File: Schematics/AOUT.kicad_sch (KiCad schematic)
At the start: 25 parts, among them J10 Line Out, J5 Inst Out, Q1 Q_NPN_BEC, Q2 Q_NPN_BEC, U4 Opamp_Dual

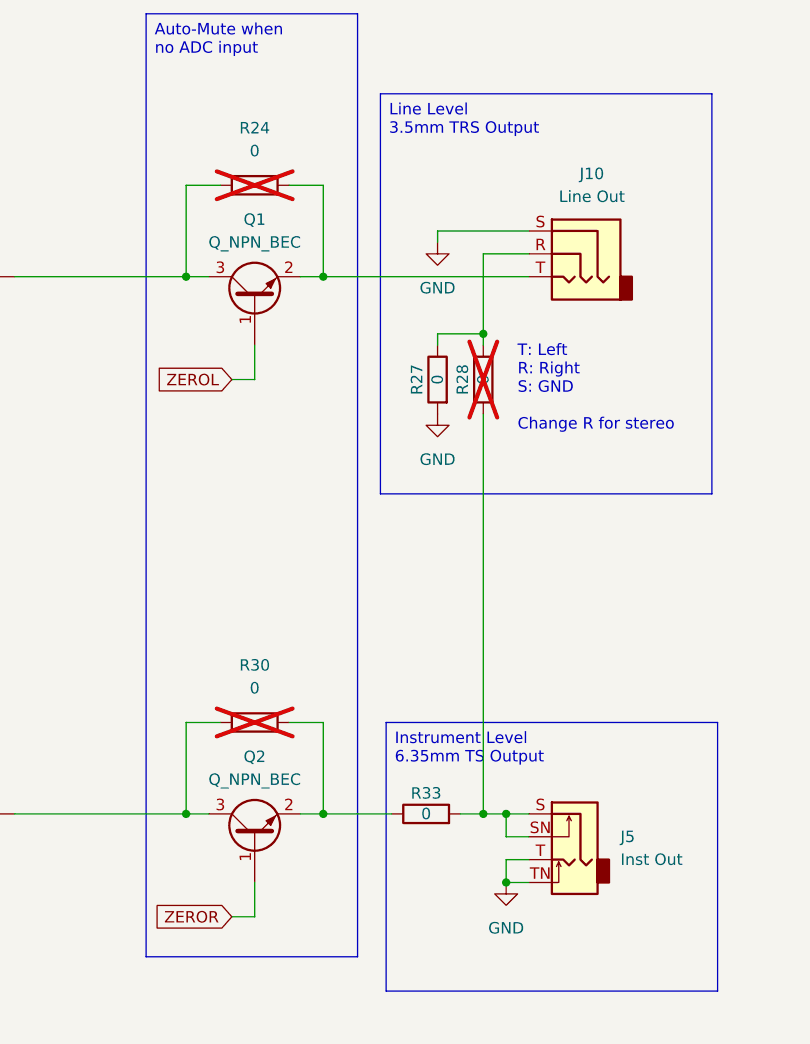
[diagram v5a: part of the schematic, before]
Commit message: Added all footprints, updated PCB
Added footprints using uni available components where possible. Might be necessary to change op-amps as they are large and not made for audio. PCB has a mockup of component placements but probably needs expanded.
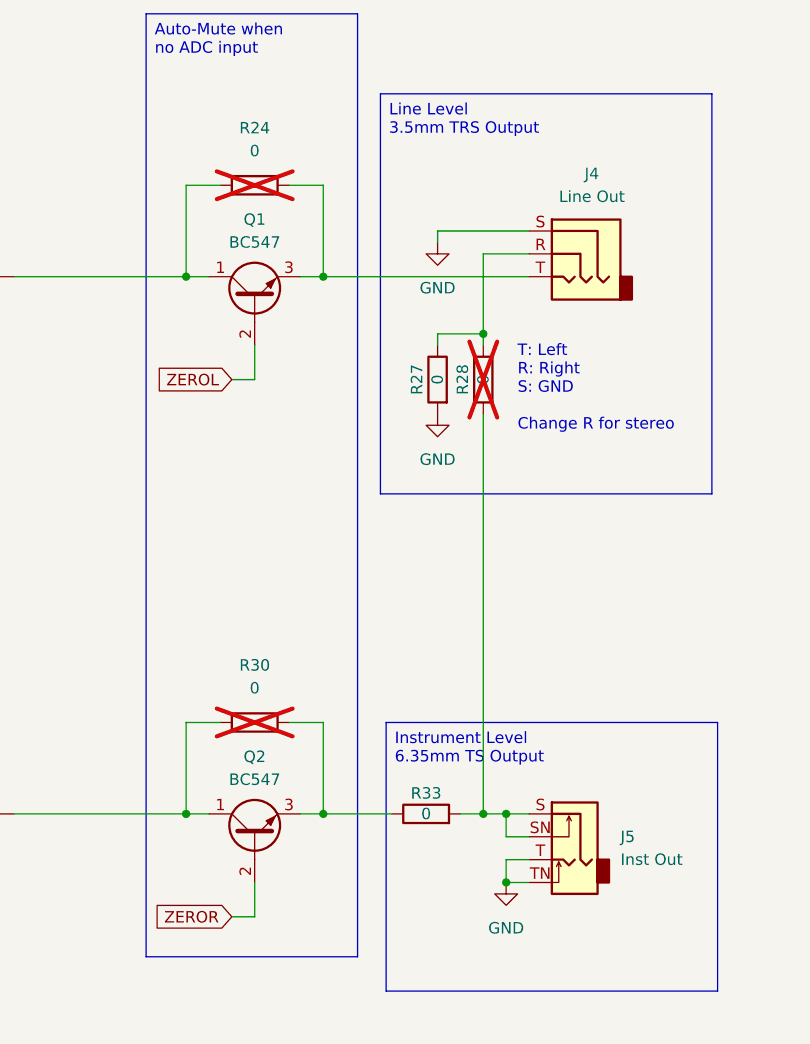
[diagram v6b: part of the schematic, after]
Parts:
- removed Q1, Q2: Q_NPN_BEC, Package_TO_SOT_THT:TO-220-3_Vertical, symbol Device:Q_NPN_BEC
- added Q1, Q2: BC547, Package_TO_SOT_THT:TO-92_Inline, symbol Transistor_BJT:BC547
- C17, C19, C20, C21, C23, C24, C25: footprint (none) -> Capacitor_SMD:C_0805_2012Metric_Pad1.18x1.45mm_HandSolder
- R23, R24, R25, R26, R27, R28, R29, R30, R31, R32, R33: footprint Resistor_SMD:R_0603_1608Metric_Pad0.98x0.95mm_HandSolder -> Resistor_SMD:R_0805_2012Metric_Pad1.20x1.40mm_HandSolder
- U4: footprint (none) -> Package_DIP:DIP-8_W7.62mm_Socket
- renumbered J10 to J4
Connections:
- net ZEROL: now also Q1.2 (B)
- net ZEROR: now also Q2.2 (B)
- net at C22.2, R30.1: now also Q2.1 (C)
- net at J4.T, R24.2: now also Q1.3 (E)
- net at C18.2, R24.1: now also Q1.1 (C)
- net at R30.2, R33.1: now also Q2.3 (E)
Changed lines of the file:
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@@
 			)
 		)
-		(property "Footprint" "Resistor_SMD:R_0603_1608Metric_Pad0.98x0.95mm_HandSolder"
+		(property "Footprint" "Resistor_SMD:R_0805_2012Metric_Pad1.20x1.40mm_HandSolder"
 			(at 178.308 78.74 90)
 			(effects
@@
 			)
 		)
-		(property "Footprint" "Resistor_SMD:R_0603_1608Metric_Pad0.98x0.95mm_HandSolder"
+		(property "Footprint" "Resistor_SMD:R_0805_2012Metric_Pad1.20x1.40mm_HandSolder"
 			(at 76.2 126.238 90)
 			(effects
@@
 			)
 		)
-		(property "Footprint" ""
+		(property "Footprint" "Capacitor_SMD:C_0805_2012Metric_Pad1.18x1.45mm_HandSolder"
 			(at 110.49 46.0248 0)
 			(effects
@@
 			)
 		)
-		(property "Footprint" "Resistor_SMD:R_0603_1608Metric_Pad0.98x0.95mm_HandSolder"
+		(property "Footprint" "Resistor_SMD:R_0805_2012Metric_Pad1.20x1.40mm_HandSolder"
 			(at 106.68 38.608 90)
 			(effects
@@
 			)
 		)
-		(property "Footprint" ""
+		(property "Footprint" "Package_DIP:DIP-8_W7.62mm_Socket"
 			(at 107.95 127 0)
 			(effects
@@
 			)
 		)
-		(property "Footprint" ""
+		(property "Footprint" "Package_DIP:DIP-8_W7.62mm_Socket"
 			(at 107.95 67.31 0)
 			(effects
@@
 	)
 	(symbol
-		(lib_id "Device:Q_NPN_BEC")
-		(at 156.21 69.85 90)
-		(unit 1)
-		(exclude_from_sim no)
-		(in_bom yes)
-		(on_board yes)
-		(dnp no)
-		(fields_autoplaced yes)
-		(property "Reference" "Q1"
-			(at 156.21 60.96 90)
-			(effects
-				(font
-					(size 1.27 1.27)
-				)
-			)
-		)
-		(property "Value" "Q_NPN_BEC"
-			(at 156.21 63.5 90)
-			(effects
-				(font
-					(size 1.27 1.27)
-				)
-			)
-		)
-		(property "Footprint" "Package_TO_SOT_THT:TO-220-3_Vertical"
-			(at 153.67 64.77 0)
-			(effects
-				(font
-					(size 1.27 1.27)
-				)
-				(hide yes)
-			)
-		)
-		(property "Datasheet" "~"
-			(at 156.21 69.85 0)
-			(effects
-				(font
-					(size 1.27 1.27)
-				)
-				(hide yes)
-			)
-		)
-		(property "Description" "NPN transistor, base/emitter/collector"
-			(at 156.21 69.85 0)
-			(effects
-				(font
-					(size 1.27 1.27)
-				)
-				(hide yes)
-			)
-		)
-		(pin "1"
-		)
-		(pin "2"
-		)
-		(pin "3"
-		)
-		(instances
-			(project "Harmoniser HAT"
-				(path "/41751dd2-97f9-4cc6-b9e6-b561e5949053/95a9c2d0-fcb3-47f7-96a1-b730c3ba5238"
-					(reference "Q1")
-					(unit 1)
-				)
-			)
-		)
-	)
-	(symbol
 		(lib_id "Device:R")
 		(at 156.21 57.15 90)
@@
 			)
 		)
-		(property "Footprint" "Resistor_SMD:R_0603_1608Metric_Pad0.98x0.95mm_HandSolder"
+		(property "Footprint" "Resistor_SMD:R_0805_2012Metric_Pad1.20x1.40mm_HandSolder"
 			(at 156.21 58.928 90)
 			(effects
@@
 			)
 		)
-		(property "Footprint" ""
+		(property "Footprint" "Capacitor_SMD:C_0805_2012Metric_Pad1.18x1.45mm_HandSolder"
 			(at 83.5152 142.24 0)
 			(effects
@@
 			)
 		)
-		(property "Footprint" ""
+		(property "Footprint" "Package_DIP:DIP-8_W7.62mm_Socket"
 			(at 66.04 176.53 0)
 			(effects
@@
 	)
 	(symbol
-		(lib_id "Device:Q_NPN_BEC")
-		(at 156.21 129.54 90)
-		(unit 1)
-		(exclude_from_sim no)
-		(in_bom yes)
-		(on_board yes)
-		(dnp no)
-		(fields_autoplaced yes)
-		(property "Reference" "Q2"
-			(at 156.21 120.65 90)
-			(effects
-				(font
-					(size 1.27 1.27)
-				)
-			)
-		)
-		(property "Value" "Q_NPN_BEC"
-			(at 156.21 123.19 90)
-			(effects
-				(font
-					(size 1.27 1.27)
-				)
-			)
-		)
-		(property "Footprint" "Package_TO_SOT_THT:TO-220-3_Vertical"
-			(at 153.67 124.46 0)
-			(effects
-				(font
-					(size 1.27 1.27)
-				)
-				(hide yes)
-			)
-		)
-		(property "Datasheet" "~"
-			(at 156.21 129.54 0)
-			(effects
-				(font
-					(size 1.27 1.27)
-				)
-				(hide yes)
-			)
-		)
-		(property "Description" "NPN transistor, base/emitter/collector"
-			(at 156.21 129.54 0)
-			(effects
-				(font
-					(size 1.27 1.27)
-				)
-				(hide yes)
-			)
-		)
-		(pin "1"
-		)
-		(pin "2"
-		)
-		(pin "3"
-		)
-		(instances
-			(project "Harmoniser HAT"
-				(path "/41751dd2-97f9-4cc6-b9e6-b561e5949053/95a9c2d0-fcb3-47f7-96a1-b730c3ba5238"
-					(reference "Q2")
-					(unit 1)
-				)
-			)
-		)
-	)
-	(symbol
 		(lib_id "Device:R")
 		(at 90.17 64.77 90)
@@
 			)
 		)
-		(property "Footprint" "Resistor_SMD:R_0603_1608Metric_Pad0.98x0.95mm_HandSolder"
+		(property "Footprint" "Resistor_SMD:R_0805_2012Metric_Pad1.20x1.40mm_HandSolder"
 			(at 90.17 66.548 90)
 			(effects
@@
 			)
 		)
-		(property "Footprint" "Resistor_SMD:R_0603_1608Metric_Pad0.98x0.95mm_HandSolder"
+		(property "Footprint" "Resistor_SMD:R_0805_2012Metric_Pad1.20x1.40mm_HandSolder"
 			(at 183.388 78.74 90)
 			(effects
@@
 			)
 		)
-		(property "Footprint" ""
+		(property "Footprint" "Capacitor_SMD:C_0805_2012Metric_Pad1.18x1.45mm_HandSolder"
 			(at 94.9452 142.24 0)
 			(effects
@@
 			)
 		)
-		(property "Footprint" "Resistor_SMD:R_0603_1608Metric_Pad0.98x0.95mm_HandSolder"
+		(property "Footprint" "Resistor_SMD:R_0805_2012Metric_Pad1.20x1.40mm_HandSolder"
 			(at 106.68 98.298 90)
 			(effects
@@
 			)
 		)
-		(property "Footprint" "Resistor_SMD:R_0603_1608Metric_Pad0.98x0.95mm_HandSolder"
+		(property "Footprint" "Resistor_SMD:R_0805_2012Metric_Pad1.20x1.40mm_HandSolder"
 			(at 156.21 118.618 90)
 			(effects
@@
 			)
 		)
-		(property "Footprint" ""
+		(property "Footprint" "Capacitor_SMD:C_0805_2012Metric_Pad1.18x1.45mm_HandSolder"
 			(at 83.5152 176.53 0)
 			(effects
@@
 			)
 		)
-		(property "Footprint" ""
+		(property "Footprint" "Capacitor_SMD:C_0805_2012Metric_Pad1.18x1.45mm_HandSolder"
 			(at 83.5152 82.55 0)
 			(effects
@@
 		(on_board yes)
 		(dnp no)
-		(property "Reference" "J10"
+		(property "Reference" "J4"
 			(at 193.675 55.88 0)
 			(effects
@@
 			(project "Harmoniser HAT"
 				(path "/41751dd2-97f9-4cc6-b9e6-b561e5949053/95a9c2d0-fcb3-47f7-96a1-b730c3ba5238"
-					(reference "J10")
+					(reference "J4")
 					(unit 1)
 				)
@@
 	)
 	(symbol
+		(lib_id "Transistor_BJT:BC547")
+		(at 156.21 129.54 90)
+		(unit 1)
+		(exclude_from_sim no)
+		(in_bom yes)
+		(on_board yes)
+		(dnp no)
+		(fields_autoplaced yes)
+		(property "Reference" "Q2"
+			(at 156.21 120.65 90)
+			(effects
+				(font
+					(size 1.27 1.27)
+				)
+			)
+		)
+		(property "Value" "BC547"
+			(at 156.21 123.19 90)
+			(effects
+				(font
+					(size 1.27 1.27)
+				)
+			)
+		)
+		(property "Footprint" "Package_TO_SOT_THT:TO-92_Inline"
+			(at 158.115 124.46 0)
+			(effects
+				(font
+					(size 1.27 1.27)
+					(italic yes)
+				)
+				(justify left)
+				(hide yes)
+			)
+		)
+		(property "Datasheet" "https://www.onsemi.com/pub/Collateral/BC550-D.pdf"
+			(at 156.21 129.54 0)
+			(effects
+				(font
+					(size 1.27 1.27)
+				)
+				(justify left)
+				(hide yes)
+			)
+		)
+		(property "Description" "0.1A Ic, 45V Vce, Small Signal NPN Transistor, TO-92"
+			(at 156.21 129.54 0)
+			(effects
+				(font
+					(size 1.27 1.27)
+				)
+				(hide yes)
+			)
+		)
+		(pin "2"
+		)
+		(pin "1"
+		)
+		(pin "3"
+		)
+		(instances
+			(project "Harmoniser HAT"
+				(path "/41751dd2-97f9-4cc6-b9e6-b561e5949053/95a9c2d0-fcb3-47f7-96a1-b730c3ba5238"
+					(reference "Q2")
+					(unit 1)
+				)
+			)
+		)
+	)
+	(symbol
 		(lib_id "power:VCOM")
 		(at 57.15 129.54 0)
@@
 			)
 		)
-		(property "Footprint" "Resistor_SMD:R_0603_1608Metric_Pad0.98x0.95mm_HandSolder"
+		(property "Footprint" "Resistor_SMD:R_0805_2012Metric_Pad1.20x1.40mm_HandSolder"
 			(at 175.26 128.778 90)
 			(effects
@@
 			)
 		)
-		(property "Footprint" "Resistor_SMD:R_0603_1608Metric_Pad0.98x0.95mm_HandSolder"
+		(property "Footprint" "Resistor_SMD:R_0805_2012Metric_Pad1.20x1.40mm_HandSolder"
 			(at 76.2 66.548 90)
 			(effects
@@
 	)
 	(symbol
+		(lib_id "Transistor_BJT:BC547")
+		(at 156.21 69.85 90)
+		(unit 1)
+		(exclude_from_sim no)
+		(in_bom yes)
+		(on_board yes)
+		(dnp no)
+		(fields_autoplaced yes)
+		(property "Reference" "Q1"
+			(at 156.21 60.96 90)
+			(effects
+				(font
+					(size 1.27 1.27)
+				)
+			)
+		)
+		(property "Value" "BC547"
+			(at 156.21 63.5 90)
+			(effects
+				(font
+					(size 1.27 1.27)
+				)
+			)
+		)
+		(property "Footprint" "Package_TO_SOT_THT:TO-92_Inline"
+			(at 158.115 64.77 0)
+			(effects
+				(font
+					(size 1.27 1.27)
+					(italic yes)
+				)
+				(justify left)
+				(hide yes)
+			)
+		)
+		(property "Datasheet" "https://www.onsemi.com/pub/Collateral/BC550-D.pdf"
+			(at 156.21 69.85 0)
+			(effects
+				(font
+					(size 1.27 1.27)
+				)
+				(justify left)
+				(hide yes)
+			)
+		)
+		(property "Description" "0.1A Ic, 45V Vce, Small Signal NPN Transistor, TO-92"
+			(at 156.21 69.85 0)
+			(effects
+				(font
+					(size 1.27 1.27)
+				)
+				(hide yes)
+			)
+		)
+		(pin "2"
+		)
+		(pin "1"
+		)
+		(pin "3"
+		)
+		(instances
+			(project ""
+				(path "/41751dd2-97f9-4cc6-b9e6-b561e5949053/95a9c2d0-fcb3-47f7-96a1-b730c3ba5238"
+					(reference "Q1")
+					(unit 1)
+				)
+			)
+		)
+	)
+	(symbol
 		(lib_id "Device:R")
 		(at 90.17 124.46 90)
@@
 			)
 		)
-		(property "Footprint" "Resistor_SMD:R_0603_1608Metric_Pad0.98x0.95mm_HandSolder"
+		(property "Footprint" "Resistor_SMD:R_0805_2012Metric_Pad1.20x1.40mm_HandSolder"
 			(at 90.17 126.238 90)
 			(effects
@@
 			)
 		)
-		(property "Footprint" ""
+		(property "Footprint" "Capacitor_SMD:C_0805_2012Metric_Pad1.18x1.45mm_HandSolder"
 			(at 110.49 105.7148 0)
 			(effects
@@
 			)
 		)
-		(property "Footprint" ""
+		(property "Footprint" "Capacitor_SMD:C_0805_2012Metric_Pad1.18x1.45mm_HandSolder"
 			(at 94.9452 82.55 0)
 			(effects

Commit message: Adjusted Capacitor Footprints
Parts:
- C18, C22: footprint Capacitor_SMD:CP_Elec_5x5.4 -> Capacitor_SMD:CP_Elec_4x5.7
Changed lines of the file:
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@@
 			)
 		)
-		(property "Footprint" "Capacitor_SMD:CP_Elec_5x5.4"
+		(property "Footprint" "Capacitor_SMD:CP_Elec_4x5.7"
 			(at 129.54 126.0348 0)
 			(effects
@@
 			)
 		)
-		(property "Footprint" "Capacitor_SMD:CP_Elec_5x5.4"
+		(property "Footprint" "Capacitor_SMD:CP_Elec_4x5.7"
 			(at 129.54 66.3448 0)
 			(effects

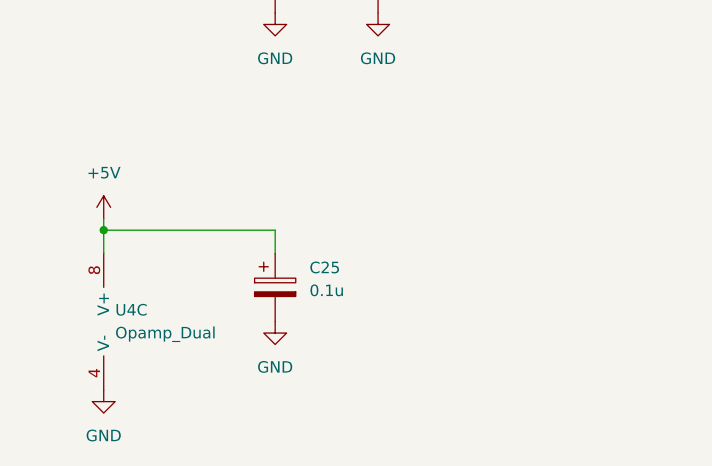
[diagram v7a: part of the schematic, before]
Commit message: Changed footprints, added 3d model to GPIO
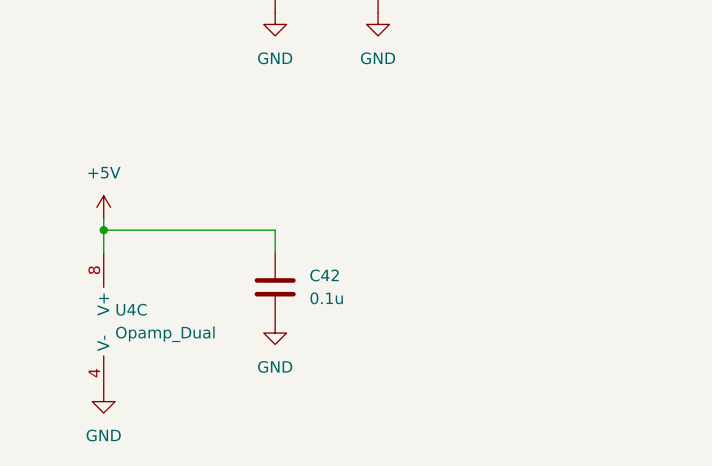
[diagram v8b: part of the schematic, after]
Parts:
- removed C25: 0.1u, Capacitor_SMD:C_0805_2012Metric_Pad1.18x1.45mm_HandSolder, symbol Device:C_Polarized
- added C42: 0.1u, Capacitor_SMD:C_0805_2012Metric_Pad1.18x1.45mm_HandSolder, symbol Device:C
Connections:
- net +5V: now also C42.1
- net GND: now also C42.2
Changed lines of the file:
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@@
+	)
+	(symbol
+		(lib_id "Device:C")
+		(at 82.55 172.72 0)
+		(unit 1)
+		(exclude_from_sim no)
+		(in_bom yes)
+		(on_board yes)
+		(dnp no)
+		(fields_autoplaced yes)
+		(property "Reference" "C42"
+			(at 86.36 171.4499 0)
+			(effects
+				(font
+					(size 1.27 1.27)
+				)
+				(justify left)
+			)
+		)
+		(property "Value" "0.1u"
+			(at 86.36 173.9899 0)
+			(effects
+				(font
+					(size 1.27 1.27)
+				)
+				(justify left)
+			)
+		)
+		(property "Footprint" "Capacitor_SMD:C_0805_2012Metric_Pad1.18x1.45mm_HandSolder"
+			(at 83.5152 176.53 0)
+			(effects
+				(font
+					(size 1.27 1.27)
+				)
+				(hide yes)
+			)
+		)
+		(property "Datasheet" "~"
+			(at 82.55 172.72 0)
+			(effects
+				(font
+					(size 1.27 1.27)
+				)
+				(hide yes)
+			)
+		)
+		(property "Description" "Unpolarized capacitor"
+			(at 82.55 172.72 0)
+			(effects
+				(font
+					(size 1.27 1.27)
+				)
+				(hide yes)
+			)
+		)
+		(pin "1"
+		)
+		(pin "2"
+		)
+		(instances
+			(project "Harmoniser HAT"
+				(path "/41751dd2-97f9-4cc6-b9e6-b561e5949053/95a9c2d0-fcb3-47f7-96a1-b730c3ba5238"
+					(reference "C42")
+					(unit 1)
+				)
+			)
+		)
 	)
 	(symbol
@@
 					(unit 1)
 				)
-			)
-		)
-	)
-	(symbol
-		(lib_id "Device:C_Polarized")
-		(at 82.55 172.72 0)
-		(unit 1)
-		(exclude_from_sim no)
-		(in_bom yes)
-		(on_board yes)
-		(dnp no)
-		(fields_autoplaced yes)
-		(property "Reference" "C25"
-			(at 86.36 170.5609 0)
-			(effects
-				(font
-					(size 1.27 1.27)
-				)
-				(justify left)
-			)
-		)
-		(property "Value" "0.1u"
-			(at 86.36 173.1009 0)
-			(effects
-				(font
-					(size 1.27 1.27)
-				)
-				(justify left)
-			)
-		)
-		(property "Footprint" "Capacitor_SMD:C_0805_2012Metric_Pad1.18x1.45mm_HandSolder"
-			(at 83.5152 176.53 0)
-			(effects
-				(font
-					(size 1.27 1.27)
-				)
-				(hide yes)
-			)
-		)
-		(property "Datasheet" "~"
-			(at 82.55 172.72 0)
-			(effects
-				(font
-					(size 1.27 1.27)
-				)
-				(hide yes)
-			)
-		)
-		(property "Description" "Polarized capacitor"
-			(at 82.55 172.72 0)
-			(effects
-				(font
-					(size 1.27 1.27)
-				)
-				(hide yes)
-			)
-		)
-		(pin "2"
-		)
-		(pin "1"
-		)
-		(instances
-			(project "Harmoniser HAT"
-				(path "/41751dd2-97f9-4cc6-b9e6-b561e5949053/95a9c2d0-fcb3-47f7-96a1-b730c3ba5238"
-					(reference "C25")
-					(unit 1)
-				)
